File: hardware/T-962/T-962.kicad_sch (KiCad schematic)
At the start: 0 parts

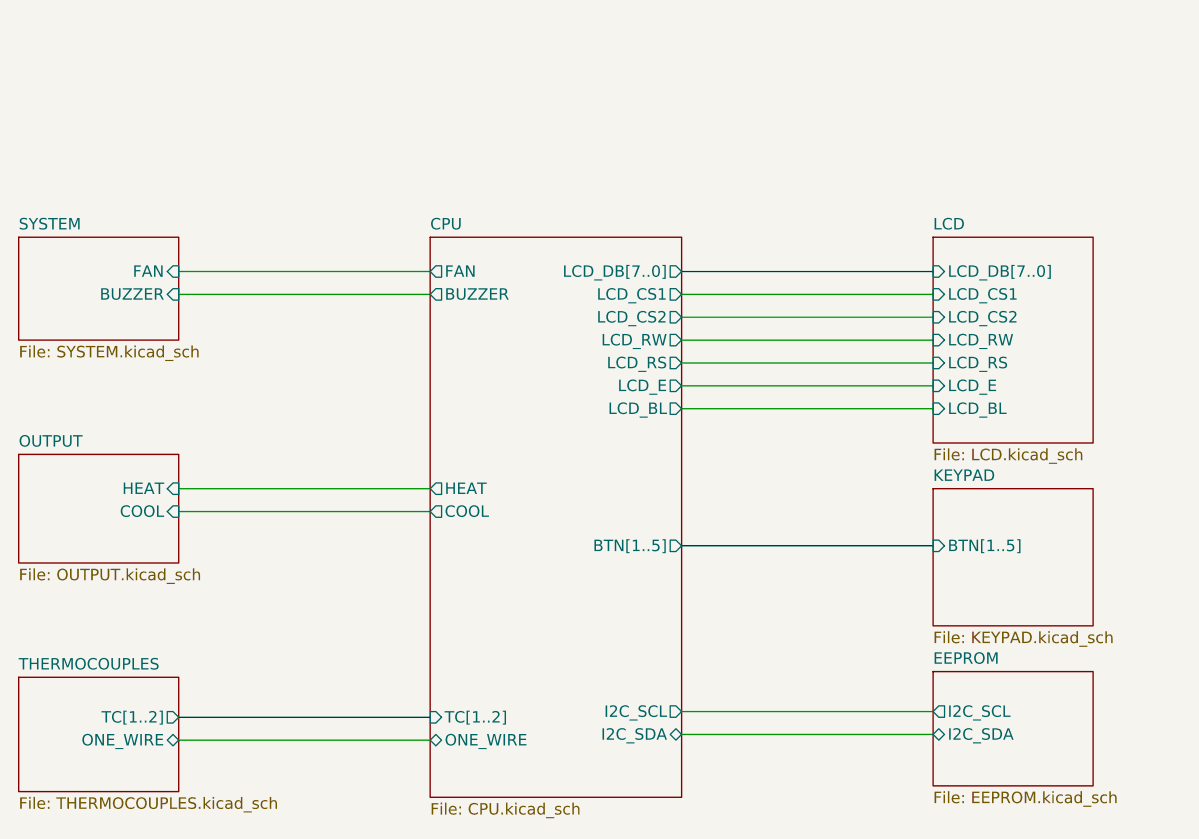
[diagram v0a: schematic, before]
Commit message: add max31850 thermocouple interfaces
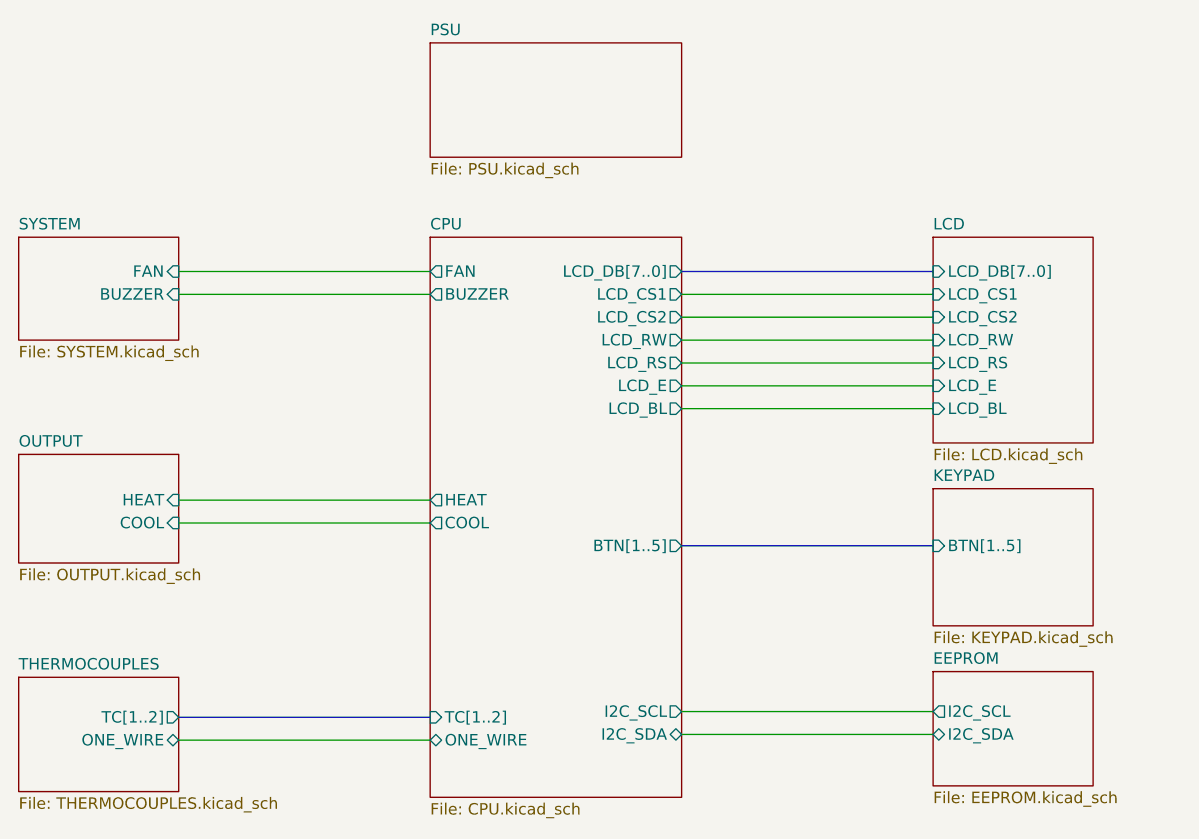
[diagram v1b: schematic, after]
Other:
- added sheet PSU (PSU.kicad_sch)
